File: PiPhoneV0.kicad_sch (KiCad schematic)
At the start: 48 parts, among them J1 GPIO, J2 TL040WVS03-H1263A, J3 Conn_01x15_MountingPin, SW1 SW_Push, SW10 SW_Push, SW11 SW_Push, SW12 SW_Push, SW13 SW_Push, SW14 SW_Push, SW15 SW_Push, SW16 SW_Push, SW17 SW_Push, SW18 SW_Push, SW2 SW_Push, SW3 SW_Push, SW4 SW_Push, SW5 SW_Push, SW6 SW_Push, SW7 SW_Push, SW8 SW_Push, SW9 SW_Push, U2 TPS61165DRV

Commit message: feat: add ground plane, clean up keyboard wiring, move around connectors.
Note: still need to do length tuning on differential pairs and make sure
rgb signal will work ok in its current configuration.
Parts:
- renumbered D4 to D10, D10 to D11, D16 to D12, D5 to D13, D11 to D14, D17 to D15, D6 to D16, D12 to D17, D7 to D2, D13 to D3, D2 to D4, D8 to D5, D14 to D6, D3 to D7, D9 to D8, D15 to D9
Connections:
- net GND: now also J2.MP (MountPin), J3.MP (MountPin)
- net GPIO13/PWM1: now also D4.1 (K), D5.1 (K), D6.1 (K); no longer SW11.1, SW14.1, SW17.1, SW2.1, SW5.1, SW8.1
- net GPIO17: no longer D7.1 (K), D8.1 (K), D9.1 (K)
- net GPIO19/PCM.FS: now also D7.1 (K), D8.1 (K), D9.1 (K); no longer SW12.1, SW15.1, SW18.1, SW3.1, SW6.1, SW9.1
- net GPIO20/PCM.DIN: now also SW11.1, SW14.1, SW17.1, SW2.1, SW5.1, SW8.1
- net GPIO21/PCM.DOUT: now also SW12.1, SW15.1, SW18.1, SW3.1, SW6.1, SW9.1
- net GPIO22: no longer D13.1 (K), D14.1 (K), D15.1 (K)
- net GPIO23: no longer D16.1 (K), D17.1 (K), D18.1 (K)
- net GPIO26: now also D10.1 (K), D11.1 (K), D12.1 (K)
- net GPIO27: no longer D10.1 (K), D11.1 (K), D12.1 (K)
- net GPIO5: now also D13.1 (K), D14.1 (K), D15.1 (K); no longer D1.1 (K), D2.1 (K), D3.1 (K)
- net GPIO6: now also D1.1 (K), D2.1 (K), D3.1 (K); no longer D4.1 (K), D5.1 (K), D6.1 (K)
- net ID_SDA: now also D16.1 (K), D17.1 (K), D18.1 (K)
- net Blue0: now reaches J2.16 (DB0)
- net Blue0: now also U1.31 (DATA2); no longer U1.7 (DATA23)
- net Blue1: now reaches J2.17 (DB1)
- net Blue1: now also U1.32 (DATA3); no longer U1.6 (DATA22)
- net Blue2: now reaches J2.18 (DB2)
- net Blue2: now also U1.33 (DATA4); no longer U1.5 (DATA21)
- net Blue3: now reaches J2.19 (DB3)
- net Blue3: now also U1.34 (DATA5); no longer U1.4 (DATA20)
- net Blue4: now reaches J2.20 (DB4)
- net Blue4: now also U1.36 (DATA6); no longer U1.2 (DATA19)
- net Blue5: now reaches J2.21 (DB5)
- net Blue5: now also U1.37 (DATA7); no longer U1.1 (DATA18)
- net Green0: now reaches J2.22 (DB6)
- net Green0: now also U1.41 (DATA10); no longer U1.46 (DATA15)
- net Green1: now reaches J2.23 (DB7)
- net Green1: now also U1.42 (DATA11); no longer U1.45 (DATA14)
- net Green2: now reaches J2.24 (DB8)
- net Green2: now also U1.43 (DATA12); no longer U1.44 (DATA13)
- net Green3: now reaches J2.25 (DB9)
- net Green3: now also U1.44 (DATA13); no longer U1.43 (DATA12)
- net Green4: now reaches J2.26 (DB10)
- net Green4: now also U1.45 (DATA14); no longer U1.42 (DATA11)
- net Green5: now reaches J2.27 (DB11)
- net Green5: now also U1.46 (DATA15); no longer U1.41 (DATA10)
- net Red0: now reaches J2.28 (DB12)
- net Red0: now also U1.1 (DATA18); no longer U1.37 (DATA7)
- net Red1: now reaches J2.29 (DB13)
- net Red1: now also U1.2 (DATA19); no longer U1.36 (DATA6)
- net Red2: now reaches J2.30 (DB14)
- net Red2: now also U1.4 (DATA20); no longer U1.34 (DATA5)
- net Red3: now reaches J2.31 (DB15)
- net Red3: now also U1.5 (DATA21); no longer U1.33 (DATA4)
- net Red4: now reaches J2.32 (DB16)
- net Red4: now also U1.6 (DATA22); no longer U1.32 (DATA3)
- net Red5: now reaches J2.33 (DB17)
- net Red5: now also U1.7 (DATA23); no longer U1.31 (DATA2)
- net DA0P: now reaches J3.9 (Pin_9), U1.14 (DA0P)
- net DA0N: now reaches J3.8 (Pin_8), U1.15 (DA0N)
- net DA1P: now reaches J3.3 (Pin_3), U1.16 (DA1P)
- net DA1N: now reaches J3.2 (Pin_2), U1.17 (DA1N)
- net DACP: now reaches J3.6 (Pin_6), U1.18 (DACP)
- net DACN: now reaches J3.5 (Pin_5), U1.19 (DACN)

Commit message: chore: generate gerbers
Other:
- company: (none) -> Hiawatha Engineering
- title: (none) -> PiPhone
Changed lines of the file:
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@@
 	(paper "A2")
 	(title_block
-		(date "15 nov 2012")
+		(title "PiPhone")
+		(date "2025-08-28")
+		(rev "1")
+		(company "Hiawatha Engineering")
 	)
 	(text "Keyboard"

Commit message: chore: match components with jlpcb
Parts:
- C5: LCSC (none) -> C21120
- C6, C7: LCSC (none) -> C15849
- D1, D10, D11, D12, D13, D14, D15, D16, D17, D18, D2, D3, D4, D5, D6, D7, D8, D9: footprint Diode_SMD:D_0201_0603Metric -> Diode_SMD:D_SOD-323; LCSC (none) -> C2128
- D20: LCSC (none) -> C77337
- J2: value TL040WVS03-H1263A -> Conn_01x40_MountingPin; LCSC (none) -> C5213762
- J3: LCSC (none) -> C66660
- L1: LCSC (none) -> C9391
- R1: LCSC (none) -> C20092485
- R2: LCSC (none) -> C863039
- U1: value ~ -> ICN6211; LCSC (none) -> C246085
- U2: LCSC (none) -> C122568

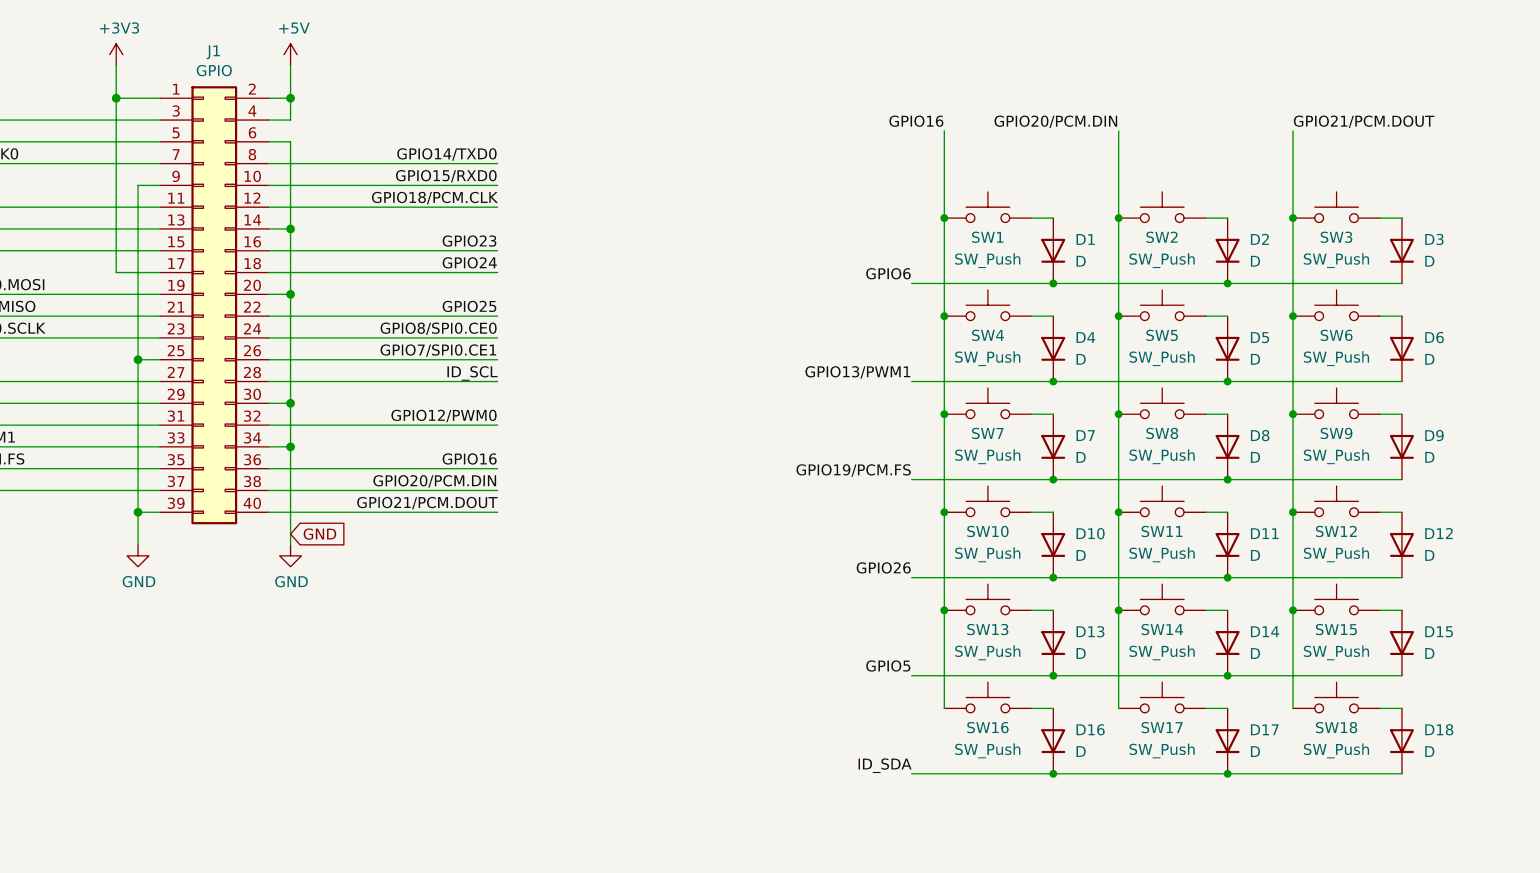
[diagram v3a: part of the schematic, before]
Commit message: chore: match parts with jlpcb
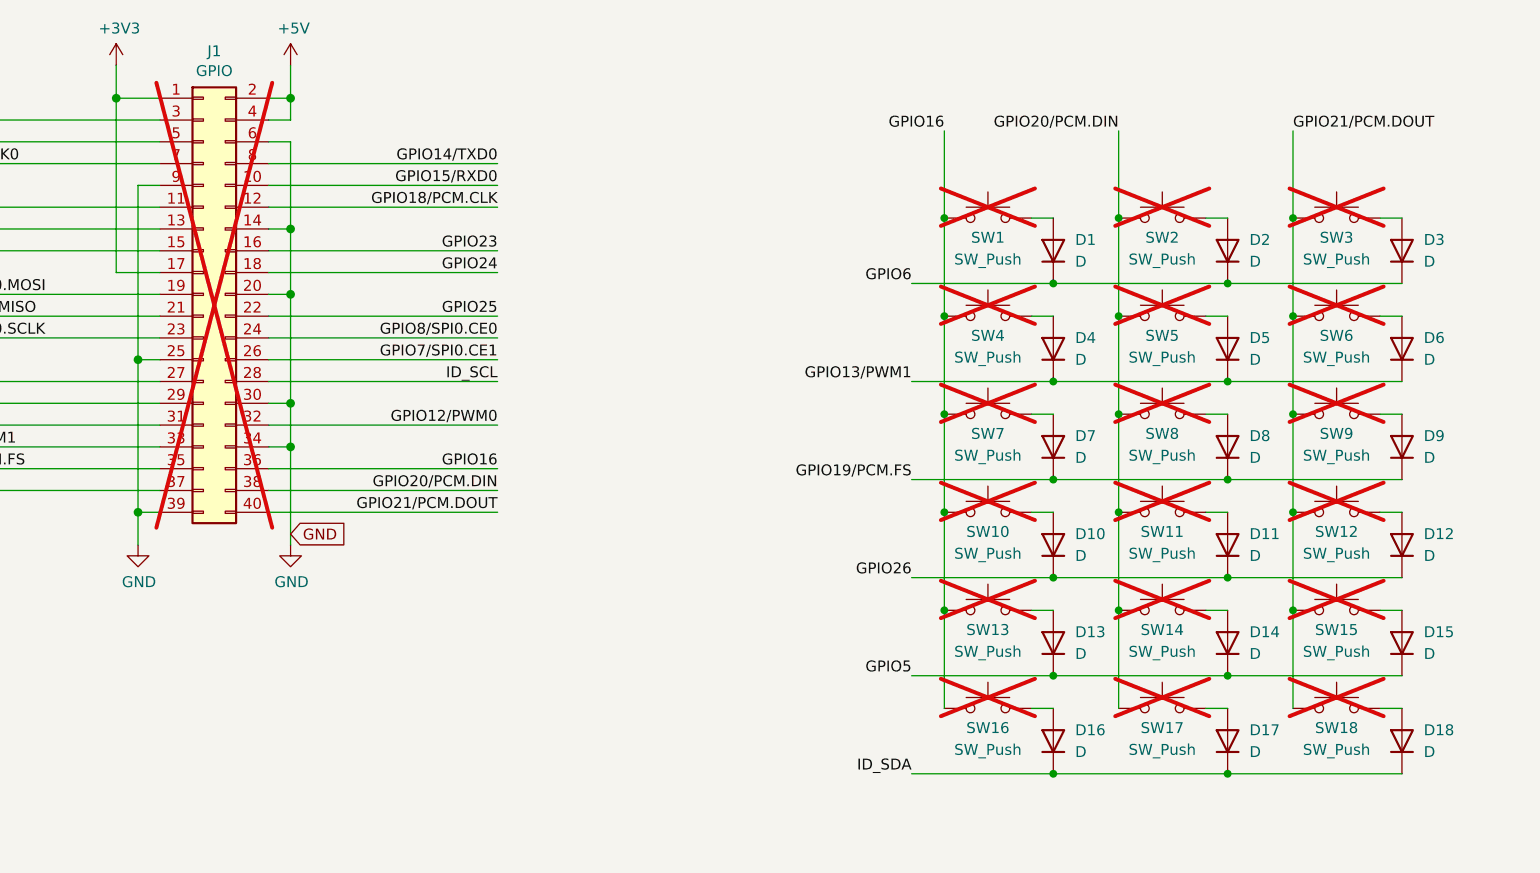
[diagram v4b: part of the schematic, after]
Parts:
- C5: LCSC C21120 -> (none); LCSC Part # (none) -> C21120
- C6, C7: LCSC C15849 -> (none); LCSC Part # (none) -> C15849
- D1, D10, D11, D12, D13, D14, D15, D16, D17, D18, D2, D3, D4, D5, D6, D7, D8, D9: LCSC C2128 -> (none); LCSC Part # (none) -> C2128
- D20: LCSC C77337 -> (none); LCSC Part # (none) -> C77337
- J1, SW1, SW10, SW11, SW12, SW13, SW14, SW15, SW16, SW17, SW18, SW2, SW3, SW4, SW5, SW6, SW7, SW8, SW9: now not fitted
- J2: LCSC C5213762 -> (none); LCSC Part # (none) -> C5213762
- J3: LCSC C66660 -> (none); LCSC Part # (none) -> C66660
- L1: LCSC C9391 -> (none); LCSC Part # (none) -> C9391
- R1: LCSC C20092485 -> (none); LCSC Part # (none) -> C20092485
- R2: LCSC C863039 -> (none); LCSC Part # (none) -> C863039
- U1: LCSC C246085 -> (none); LCSC Part # (none) -> C246085
- U2: LCSC C122568 -> (none); LCSC Part # (none) -> C122568
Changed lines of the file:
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@@
 		(in_bom yes)
 		(on_board yes)
-		(dnp no)
+		(dnp yes)
 		(property "Reference" "J1"
 			(at 67.31 22.4598 0)
@@
 		(in_bom yes)
 		(on_board yes)
-		(dnp no)
+		(dnp yes)
 		(property "Reference" "SW13"
 			(at 157.48 89.916 0)
@@
 		(in_bom yes)
 		(on_board yes)
-		(dnp no)
+		(dnp yes)
 		(property "Reference" "SW8"
 			(at 177.8 67.056 0)
@@
 			)
 		)
-		(property "LCSC" "C2128"
+		(property "LCSC Part #" "C2128"
 			(at 205.74 102.87 90)
 			(effects
@@
 			)
 		)
-		(property "LCSC" "C2128"
+		(property "LCSC Part #" "C2128"
 			(at 205.74 91.44 90)
 			(effects
@@
 		(in_bom yes)
 		(on_board yes)
-		(dnp no)
+		(dnp yes)
 		(property "Reference" "SW18"
 			(at 198.12 101.346 0)
@@
 			)
 		)
-		(property "LCSC" "C5213762"
+		(property "LCSC Part #" "C5213762"
 			(at 534.67 93.98 0)
 			(effects
@@
 		(in_bom yes)
 		(on_board yes)
-		(dnp no)
+		(dnp yes)
 		(property "Reference" "SW17"
 			(at 177.8 101.346 0)
@@
 			)
 		)
-		(property "LCSC" "C246085"
+		(property "LCSC Part #" "C246085"
 			(at 455.93 67.31 0)
 			(effects
@@
 			)
 		)
-		(property "LCSC" "C863039"
+		(property "LCSC Part #" "C863039"
 			(at 520.7 142.24 90)
 			(effects
@@
 			)
 		)
-		(property "LCSC" "C2128"
+		(property "LCSC Part #" "C2128"
 			(at 205.74 68.58 90)
 			(effects
@@
 		(in_bom yes)
 		(on_board yes)
-		(dnp no)
+		(dnp yes)
 		(property "Reference" "SW12"
 			(at 198.12 78.486 0)
@@
 			)
 		)
-		(property "LCSC" "C2128"
+		(property "LCSC Part #" "C2128"
 			(at 205.74 80.01 90)
 			(effects
@@
 		(in_bom yes)
 		(on_board yes)
-		(dnp no)
+		(dnp yes)
 		(property "Reference" "SW11"
 			(at 177.8 78.486 0)
@@
 		(in_bom yes)
 		(on_board yes)
-		(dnp no)
+		(dnp yes)
 		(property "Reference" "SW1"
 			(at 157.48 44.196 0)
@@
 		(in_bom yes)
 		(on_board yes)
-		(dnp no)
+		(dnp yes)
 		(property "Reference" "SW5"
 			(at 177.8 55.626 0)
@@
 			)
 		)
-		(property "LCSC" "C2128"
+		(property "LCSC Part #" "C2128"
 			(at 165.1 68.58 90)
 			(effects
@@
 			)
 		)
-		(property "LCSC" "C2128"
+		(property "LCSC Part #" "C2128"
 			(at 165.1 80.01 90)
 			(effects
@@
 			)
 		)
-		(property "LCSC" "C2128"
+		(property "LCSC Part #" "C2128"
 			(at 185.42 45.72 90)
 			(effects
@@
 			)
 		)
-		(property "LCSC" "C15849"
+		(property "LCSC Part #" "C15849"
 			(at 472.44 142.24 0)
 			(effects
@@
 			)
 		)
-		(property "LCSC" "C2128"
+		(property "LCSC Part #" "C2128"
 			(at 165.1 102.87 90)
 			(effects
@@
 			)
 		)
-		(property "LCSC" "C2128"
+		(property "LCSC Part #" "C2128"
 			(at 185.42 102.87 90)
 			(effects
@@
 		(in_bom yes)
 		(on_board yes)
-		(dnp no)
+		(dnp yes)
 		(property "Reference" "SW9"
 			(at 198.12 67.056 0)
@@
 			)
 		)
-		(property "LCSC" "C77337"
+		(property "LCSC Part #" "C77337"
 			(at 502.92 138.43 0)
 			(effects
@@
 			)
 		)
-		(property "LCSC" "C2128"
+		(property "LCSC Part #" "C2128"
 			(at 205.74 45.72 90)
 			(effects
@@
 			)
 		)
-		(property "LCSC" "C2128"
+		(property "LCSC Part #" "C2128"
 			(at 165.1 45.72 90)
 			(effects
@@
 			)
 		)
-		(property "LCSC" "C2128"
+		(property "LCSC Part #" "C2128"
 			(at 165.1 91.44 90)
 			(effects
@@
 		(in_bom yes)
 		(on_board yes)
-		(dnp no)
+		(dnp yes)
 		(property "Reference" "SW14"
 			(at 177.8 89.916 0)
@@
 			)
 		)
-		(property "LCSC" "C2128"
+		(property "LCSC Part #" "C2128"
 			(at 165.1 57.15 90)
 			(effects
@@
 			)
 		)
-		(property "LCSC" "C122568"
+		(property "LCSC Part #" "C122568"
 			(at 488.95 154.94 0)
 			(effects
@@
 		(in_bom yes)
 		(on_board yes)
-		(dnp no)
+		(dnp yes)
 		(property "Reference" "SW2"
 			(at 177.8 44.196 0)
@@
 			)
 		)
-		(property "LCSC" "C2128"
+		(property "LCSC Part #" "C2128"
 			(at 185.42 91.44 90)
 			(effects
@@
 			)
 		)
-		(property "LCSC" "C20092485"
+		(property "LCSC Part #" "C20092485"
 			(at 504.19 156.21 0)
 			(effects
@@
 		(in_bom yes)
 		(on_board yes)
-		(dnp no)
+		(dnp yes)
 		(property "Reference" "SW15"
 			(at 198.12 89.916 0)
@@
 		(in_bom yes)
 		(on_board yes)
-		(dnp no)
+		(dnp yes)
 		(property "Reference" "SW10"
 			(at 157.48 78.486 0)
@@
 			)
 		)
-		(property "LCSC" "C66660"
+		(property "LCSC Part #" "C66660"
 			(at 416.56 99.06 0)
 			(effects
@@
 			)
 		)
-		(property "LCSC" "C2128"
+		(property "LCSC Part #" "C2128"
 			(at 185.42 68.58 90)
 			(effects
@@
 			)
 		)
-		(property "LCSC" "C15849"
+		(property "LCSC Part #" "C15849"
 			(at 508 142.24 0)
 			(effects
@@
 		(in_bom yes)
 		(on_board yes)
-		(dnp no)
+		(dnp yes)
 		(property "Reference" "SW16"
 			(at 157.48 101.346 0)
@@
 			)
 		)
-		(property "LCSC" "C21120"
+		(property "LCSC Part #" "C21120"
 			(at 464.82 157.48 90)
 			(effects
@@
 			)
 		)
-		(property "LCSC" "C9391"
+		(property "LCSC Part #" "C9391"
 			(at 488.95 138.43 90)
 			(effects
@@
 		(in_bom yes)
 		(on_board yes)
-		(dnp no)
+		(dnp yes)
 		(property "Reference" "SW4"
 			(at 157.48 55.626 0)
@@
 			)
 		)
-		(property "LCSC" "C2128"
+		(property "LCSC Part #" "C2128"
 			(at 205.74 57.15 90)
 			(effects
@@
 			)
 		)
-		(property "LCSC" "C2128"
+		(property "LCSC Part #" "C2128"
 			(at 185.42 57.15 90)
 			(effects
@@
 		(in_bom yes)
 		(on_board yes)
-		(dnp no)
+		(dnp yes)
 		(property "Reference" "SW7"
 			(at 157.48 67.056 0)
@@
 		(in_bom yes)
 		(on_board yes)
-		(dnp no)
+		(dnp yes)
 		(property "Reference" "SW3"
 			(at 198.12 44.196 0)
@@
 			)
 		)
-		(property "LCSC" "C2128"
+		(property "LCSC Part #" "C2128"
 			(at 185.42 80.01 90)
 			(effects
@@
 		(in_bom yes)
 		(on_board yes)
-		(dnp no)
+		(dnp yes)
 		(property "Reference" "SW6"
 			(at 198.12 55.626 0)

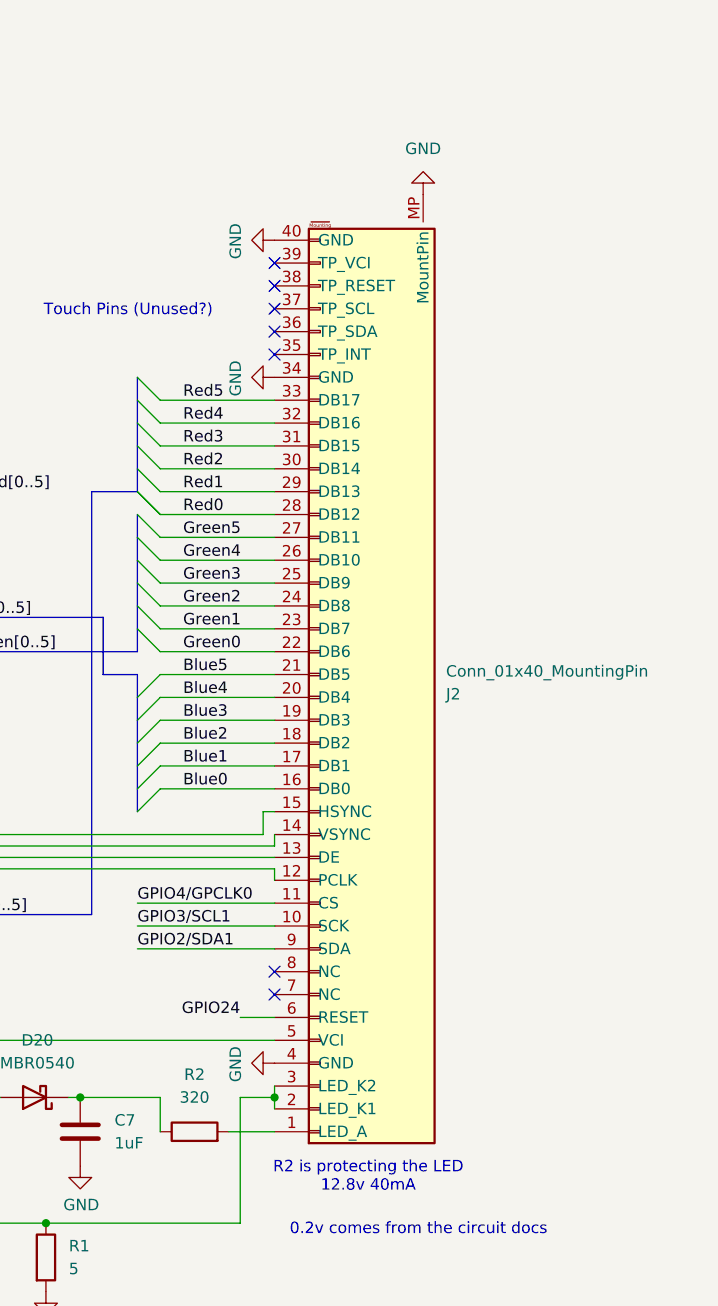
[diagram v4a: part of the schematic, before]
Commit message: feat: update adapters to match those easily on jlpcb
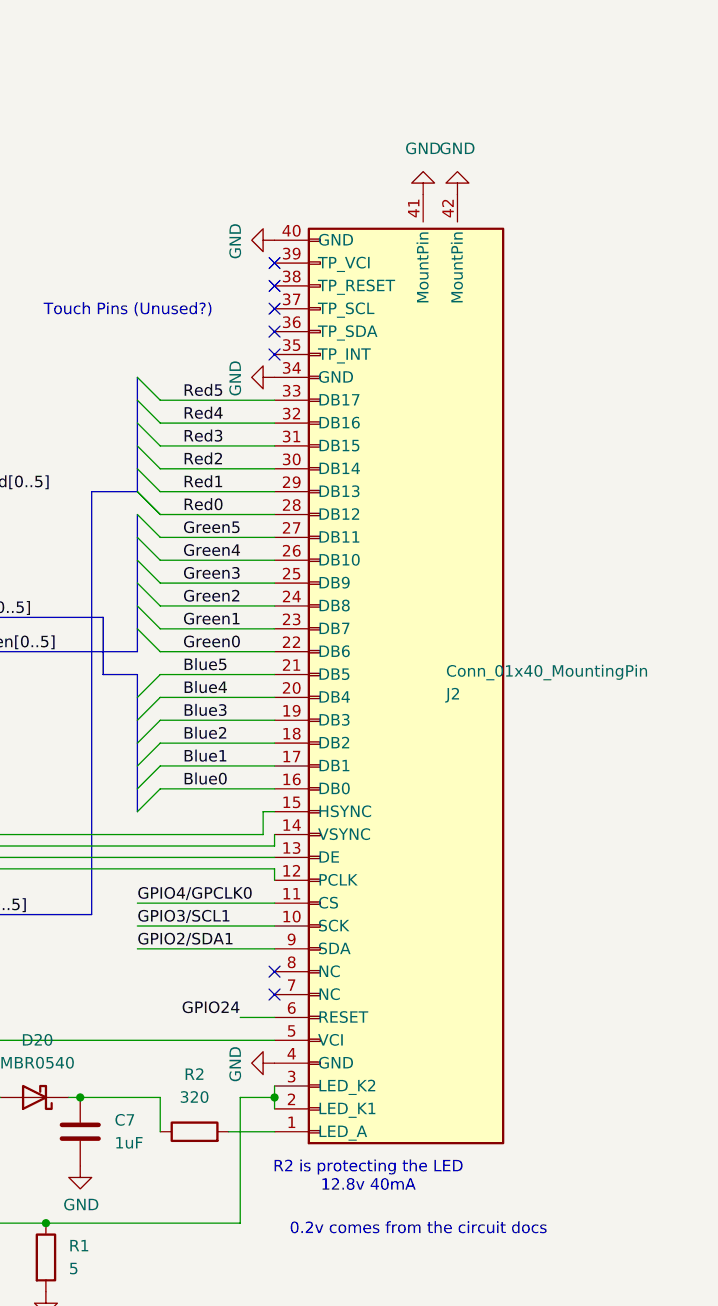
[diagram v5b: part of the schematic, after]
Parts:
- J2: footprint Connector_FFC-FPC:Hirose_FH12-40S-0.5SH_1x40-1MP_P0.50mm_Horizontal -> EasyEDA:CONN-SMD_40P-P0.50_HCTL_HC-FPC-05-09-40RLTAG
- J3: footprint Connector_FFC-FPC:Molex_200528-0150_1x15-1MP_P1.00mm_Horizontal -> EasyEDA:FPC-SMD_15P-P1.00_HDGC_1.0K-GT-15PB; LCSC Part # C66660 -> C2915527
- R1: LCSC Part # C20092485 -> C6145550
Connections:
- net GND: now also J2.41 (MountPin), J2.42 (MountPin); no longer J2.MP (MountPin)
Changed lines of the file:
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@@
 			)
 		)
-		(property "Footprint" "Connector_FFC-FPC:Hirose_FH12-40S-0.5SH_1x40-1MP_P0.50mm_Horizontal"
+		(property "Footprint" "EasyEDA:CONN-SMD_40P-P0.50_HCTL_HC-FPC-05-09-40RLTAG"
 			(at 534.67 93.98 0)
 			(effects
@@
 		(pin "6"
 		)
-		(pin "MP"
+		(pin "41"
 		)
 		(pin "5"
@@
 		)
 		(pin "39"
+		)
+		(pin "42"
 		)
 		(instances
@@
 	)
 	(symbol
+		(lib_id "power:GND")
+		(at 549.91 38.1 180)
+		(unit 1)
+		(exclude_from_sim no)
+		(in_bom yes)
+		(on_board yes)
+		(dnp no)
+		(fields_autoplaced yes)
+		(property "Reference" "#PWR07"
+			(at 549.91 31.75 0)
+			(effects
+				(font
+					(size 1.27 1.27)
+				)
+				(hide yes)
+			)
+		)
+		(property "Value" "GND"
+			(at 549.91 33.02 0)
+			(effects
+				(font
+					(size 1.27 1.27)
+				)
+			)
+		)
+		(property "Footprint" ""
+			(at 549.91 38.1 0)
+			(effects
+				(font
+					(size 1.27 1.27)
+				)
+				(hide yes)
+			)
+		)
+		(property "Datasheet" ""
+			(at 549.91 38.1 0)
+			(effects
+				(font
+					(size 1.27 1.27)
+				)
+				(hide yes)
+			)
+		)
+		(property "Description" "Power symbol creates a global label with name \"GND\" , ground"
+			(at 549.91 38.1 0)
+			(effects
+				(font
+					(size 1.27 1.27)
+				)
+				(hide yes)
+			)
+		)
+		(pin "1"
+		)
+		(instances
+			(project "PiPhoneV0"
+				(path "/e63e39d7-6ac0-4ffd-8aa3-1841a4541b55"
+					(reference "#PWR07")
+					(unit 1)
+				)
+			)
+		)
+	)
+	(symbol
 		(lib_id "Device:D")
 		(at 165.1 68.58 90)
@@
 			)
 		)
-		(property "LCSC Part #" "C20092485"
+		(property "LCSC Part #" "C6145550"
 			(at 504.19 156.21 0)
 			(effects
@@
 			)
 		)
-		(property "Footprint" "Connector_FFC-FPC:Molex_200528-0150_1x15-1MP_P1.00mm_Horizontal"
+		(property "Footprint" "EasyEDA:FPC-SMD_15P-P1.00_HDGC_1.0K-GT-15PB"
 			(at 416.56 99.06 0)
 			(effects
@@
 			)
 		)
-		(property "LCSC Part #" "C66660"
+		(property "LCSC Part #" "C2915527"
 			(at 416.56 99.06 0)
 			(effects
